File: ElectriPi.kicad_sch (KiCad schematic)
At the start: 35 parts, among them J1 2444, J2 JST XH 01x02, J3 JST XH 01x02, J6 Raspberry_Pi_2_3, J8 JST XH 01x02, Q1 30V 4A 44mΩ, Q2 50nA 150V 200mW 200mA, Q3 30V 4A 44mΩ, U1 XL4015

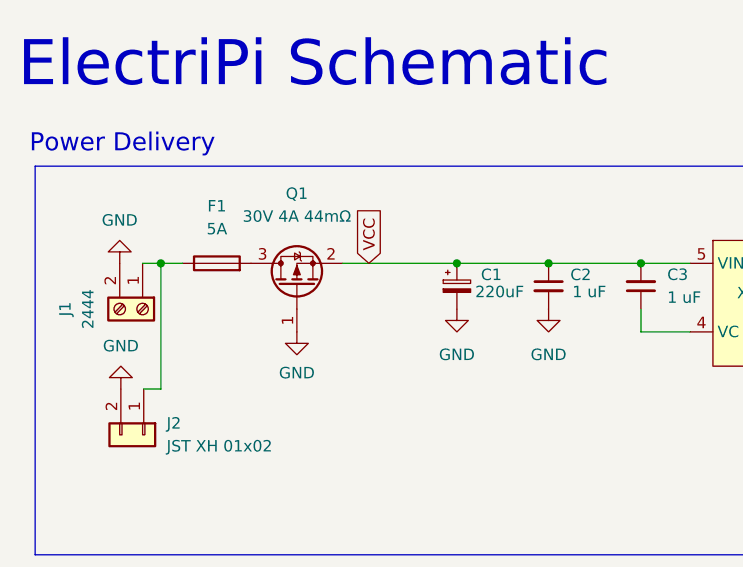
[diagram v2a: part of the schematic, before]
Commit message: Adding ICL footprint and schematic symbol
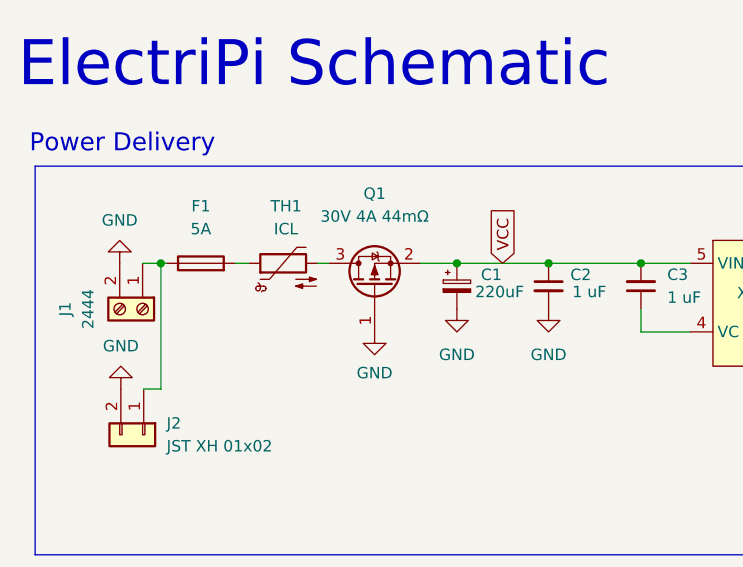
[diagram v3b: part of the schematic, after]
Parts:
- added TH1: ICL, Inrush_Limiter:5_OR_7pt5_PITCH_ICL, symbol Device:Thermistor_NTC
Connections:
- net at F1.2: now also TH1.1; no longer Q1.3 (D)
- new net: Q1.3 (D), TH1.2
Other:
- moved on the sheet: F1, Q1
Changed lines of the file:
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@@
     (stroke (width 0) (type default) (color 0 0 0 0))
   )
-  (wire (pts (xy 31.115 43.18) (xy 33.528 43.18))
+  (wire (pts (xy 31.115 43.18) (xy 31.75 43.18))
     (stroke (width 0) (type default) (color 0 0 0 0))
   )
@@
     (stroke (width 0) (type default) (color 0 0 0 0))
   )
-  (wire (pts (xy 51.308 43.18) (xy 64.008 43.18))
+  (wire (pts (xy 59.944 43.18) (xy 64.008 43.18))
     (stroke (width 0) (type default) (color 0 0 0 0))
   )
@@
     (stroke (width 0) (type default) (color 0 0 0 0))
   )
+  (wire (pts (xy 48.514 43.18) (xy 49.784 43.18))
+    (stroke (width 0) (type default) (color 0 0 0 0))
+  )
   (polyline (pts (xy 17.78 167.005) (xy 55.88 167.005))
     (stroke (width 0) (type default) (color 0 0 0 0))
@@
   )
   (wire (pts (xy 84.455 43.18) (xy 89.916 43.18))
+    (stroke (width 0) (type default) (color 0 0 0 0))
+  )
+  (wire (pts (xy 39.37 43.18) (xy 40.894 43.18))
     (stroke (width 0) (type default) (color 0 0 0 0))
   )
@@
     )
   )
-  (global_label "VCC" (shape input) (at 54.229 43.18 90) (fields_autoplaced)
+  (global_label "VCC" (shape input) (at 69.088 43.18 90) (fields_autoplaced)
     (effects (font (size 1.27 1.27)) (justify left))
-    (property "Intersheet References" "${INTERSHEET_REFS}" (id 0) (at 54.1496 37.1383 90)
+    (property "Intersheet References" "${INTERSHEET_REFS}" (id 0) (at 69.0086 37.1383 90)
       (effects (font (size 1.27 1.27)) (justify left) hide)
     )
@@
     (pin "2")
   )
-  (symbol (lib_id "power:GND") (at 46.228 50.8 0) (unit 1)
-    (in_bom yes) (on_board yes) (fields_autoplaced)
-    (property "Reference" "#PWR02" (id 0) (at 46.228 57.15 0)
-      (effects (font (size 1.27 1.27)) hide)
-    )
-    (property "Value" "GND" (id 1) (at 46.228 55.372 0))
-    (property "Footprint" "" (id 2) (at 46.228 50.8 0)
-      (effects (font (size 1.27 1.27)) hide)
-    )
-    (property "Datasheet" "" (id 3) (at 46.228 50.8 0)
-      (effects (font (size 1.27 1.27)) hide)
-    )
-    (pin "1")
+  (symbol (lib_id "power:GND") (at 54.864 50.8 0) (unit 1)
+    (in_bom yes) (on_board yes) (fields_autoplaced)
+    (property "Reference" "#PWR02" (id 0) (at 54.864 57.15 0)
+      (effects (font (size 1.27 1.27)) hide)
+    )
+    (property "Value" "GND" (id 1) (at 54.864 55.372 0))
+    (property "Footprint" "" (id 2) (at 54.864 50.8 0)
+      (effects (font (size 1.27 1.27)) hide)
+    )
+    (property "Datasheet" "" (id 3) (at 54.864 50.8 0)
+      (effects (font (size 1.27 1.27)) hide)
+    )
+    (pin "1")
+  )
+  (symbol (lib_id "Device:Thermistor_NTC") (at 44.704 43.18 90) (unit 1)
+    (in_bom yes) (on_board yes) (fields_autoplaced)
+    (property "Reference" "TH1" (id 0) (at 45.0215 36.83 90))
+    (property "Value" "ICL" (id 1) (at 45.0215 39.37 90))
+    (property "Footprint" "Inrush_Limiter:5_OR_7pt5_PITCH_ICL" (id 2) (at 43.434 43.18 0)
+      (effects (font (size 1.27 1.27)) hide)
+    )
+    (property "Datasheet" "~" (id 3) (at 43.434 43.18 0)
+      (effects (font (size 1.27 1.27)) hide)
+    )
+    (pin "1")
+    (pin "2")
   )
   (symbol (lib_id "power:GND") (at 29.083 150.622 270) (unit 1)
@@
     (pin "5")
   )
-  (symbol (lib_id "Device:Fuse") (at 37.338 43.18 90) (unit 1)
-    (in_bom yes) (on_board yes) (fields_autoplaced)
-    (property "Reference" "F1" (id 0) (at 37.338 36.83 90))
-    (property "Value" "5A" (id 1) (at 37.338 39.37 90))
-    (property "Footprint" "Fuse:Fuse_Littelfuse-NANO2-451_453" (id 2) (at 37.338 44.958 90)
-      (effects (font (size 1.27 1.27)) hide)
-    )
-    (property "Datasheet" "~" (id 3) (at 37.338 43.18 0)
-      (effects (font (size 1.27 1.27)) hide)
-    )
-    (property "LCSC" "C108518" (id 4) (at 37.338 43.18 90)
-      (effects (font (size 1.27 1.27)) hide)
-    )
-    (property "PCBway" "" (id 5) (at 37.338 43.18 0)
-      (effects (font (size 1.27 1.27)) hide)
-    )
-    (property "abv.Footprint" "" (id 6) (at 37.338 43.18 0)
-      (effects (font (size 1.27 1.27)) hide)
-    )
-    (property "ManfNum" "" (id 7) (at 37.338 43.18 0)
+  (symbol (lib_id "Device:Fuse") (at 35.56 43.18 90) (unit 1)
+    (in_bom yes) (on_board yes) (fields_autoplaced)
+    (property "Reference" "F1" (id 0) (at 35.56 36.83 90))
+    (property "Value" "5A" (id 1) (at 35.56 39.37 90))
+    (property "Footprint" "Fuse:Fuse_Littelfuse-NANO2-451_453" (id 2) (at 35.56 44.958 90)
+      (effects (font (size 1.27 1.27)) hide)
+    )
+    (property "Datasheet" "~" (id 3) (at 35.56 43.18 0)
+      (effects (font (size 1.27 1.27)) hide)
+    )
+    (property "LCSC" "C108518" (id 4) (at 35.56 43.18 90)
+      (effects (font (size 1.27 1.27)) hide)
+    )
+    (property "PCBway" "" (id 5) (at 35.56 43.18 0)
+      (effects (font (size 1.27 1.27)) hide)
+    )
+    (property "abv.Footprint" "" (id 6) (at 35.56 43.18 0)
+      (effects (font (size 1.27 1.27)) hide)
+    )
+    (property "ManfNum" "" (id 7) (at 35.56 43.18 0)
       (effects (font (size 1.27 1.27)) hide)
     )
@@
     (pin "1")
   )
-  (symbol (lib_id "Transistor_FET:AO3401A") (at 46.228 45.72 90) (unit 1)
-    (in_bom yes) (on_board yes) (fields_autoplaced)
-    (property "Reference" "Q1" (id 0) (at 46.228 35.433 90))
-    (property "Value" "30V 4A 44mΩ" (id 1) (at 46.228 37.973 90))
-    (property "Footprint" "Package_TO_SOT_SMD:SOT-23" (id 2) (at 48.133 40.64 0)
+  (symbol (lib_id "Transistor_FET:AO3401A") (at 54.864 45.72 90) (unit 1)
+    (in_bom yes) (on_board yes) (fields_autoplaced)
+    (property "Reference" "Q1" (id 0) (at 54.864 35.433 90))
+    (property "Value" "30V 4A 44mΩ" (id 1) (at 54.864 37.973 90))
+    (property "Footprint" "Package_TO_SOT_SMD:SOT-23" (id 2) (at 56.769 40.64 0)
       (effects (font (size 1.27 1.27) italic) (justify left) hide)
     )
-    (property "Datasheet" "http://www.aosmd.com/pdfs/datasheet/AO3401A.pdf" (id 3) (at 46.228 45.72 0)
+    (property "Datasheet" "http://www.aosmd.com/pdfs/datasheet/AO3401A.pdf" (id 3) (at 54.864 45.72 0)
       (effects (font (size 1.27 1.27)) (justify left) hide)
     )
-    (property "LCSC" "C15127" (id 4) (at 46.228 45.72 0)
-      (effects (font (size 1.27 1.27)) hide)
-    )
-    (property "ManfNum" "AO3401A" (id 5) (at 46.228 45.72 0)
-      (effects (font (size 1.27 1.27)) hide)
-    )
-    (property "abv.Footprint" "SOT-23" (id 6) (at 46.228 45.72 0)
+    (property "LCSC" "C15127" (id 4) (at 54.864 45.72 0)
+      (effects (font (size 1.27 1.27)) hide)
+    )
+    (property "ManfNum" "AO3401A" (id 5) (at 54.864 45.72 0)
+      (effects (font (size 1.27 1.27)) hide)
+    )
+    (property "abv.Footprint" "SOT-23" (id 6) (at 54.864 45.72 0)
       (effects (font (size 1.27 1.27)) hide)
     )
@@
       (reference "R10") (unit 1) (value "10K") (footprint "Resistor_SMD:R_0603_1608Metric")
     )
+    (path "/6bddfc29-f374-41df-b0b6-4faa72e48167"
+      (reference "TH1") (unit 1) (value "ICL") (footprint "Inrush_Limiter:5_OR_7pt5_PITCH_ICL")
+    )
     (path "/b1afdc82-ee5a-4cef-b119-9cb72898d220"

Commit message: adding test points
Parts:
- added TP1, TP2, TP3, TP4, TP5: TestPoint, TestPoint:TestPoint_Pad_D1.5mm, symbol Connector:TestPoint
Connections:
- net +5V: now also TP1.1
- net 5V_PI: now also TP5.1
- net VCC: now also TP4.1
- net at F1.1, J1.1 (Pin_1), J2.1 (Pin_1): now also TP2.1
- net at Q1.3 (D), TH1.2: now also TP3.1
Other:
- note removed: "add test points add 5V barrier block"
- moved on the sheet: F1, J1, J2, TH1

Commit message: small BOM updates
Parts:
- J1: LCSC (none) -> C123214
- J2, J3, J8: LCSC (none) -> C492456
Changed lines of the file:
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@@
       (effects (font (size 1.27 1.27)) hide)
     )
-    (property "LCSC" "" (id 4) (at 146.05 93.98 90)
+    (property "LCSC" "C492456" (id 4) (at 146.05 93.98 90)
       (effects (font (size 1.27 1.27)) hide)
     )
@@
       (effects (font (size 1.27 1.27)) hide)
     )
-    (property "LCSC" "" (id 4) (at 27.178 48.26 0)
+    (property "LCSC" "C123214" (id 4) (at 27.178 48.26 0)
       (effects (font (size 1.27 1.27)) hide)
     )
@@
     )
     (property "Datasheet" "~" (id 3) (at 27.178 62.738 0)
+      (effects (font (size 1.27 1.27)) hide)
+    )
+    (property "LCSC" "C492456" (id 4) (at 27.178 62.738 0)
       (effects (font (size 1.27 1.27)) hide)
     )
@@
       (effects (font (size 1.27 1.27)) hide)
     )
+    (property "LCSC" "C492456" (id 5) (at 161.925 151.765 0)
+      (effects (font (size 1.27 1.27)) hide)
+    )

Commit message: Adding Mouser part number for ICL
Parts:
- TH1: Mouser (none) -> 871-B57238S0709M000
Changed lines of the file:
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@@
       (effects (font (size 1.27 1.27)) hide)
     )
-    (property "Datasheet" "~" (id 3) (at 40.894 43.18 0)
+    (property "Datasheet" "https://product.tdk.com/system/files/dam/doc/product/protection/current/ntc-limiter/data_sheet/50/db/icl_16/s238.pdf" (id 3) (at 40.894 43.18 0)
       (effects (font (size 1.27 1.27)) hide)
     )
+    (property "Mouser" " 871-B57238S0709M000" (id 4) (at 42.164 43.18 90)
+      (effects (font (size 1.27 1.27)) hide)
+    )

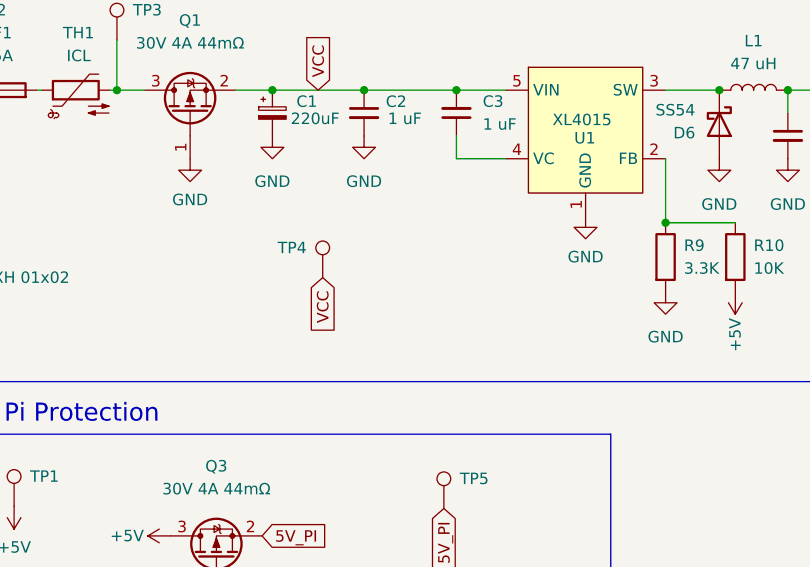
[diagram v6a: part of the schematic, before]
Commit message: adding GND test point
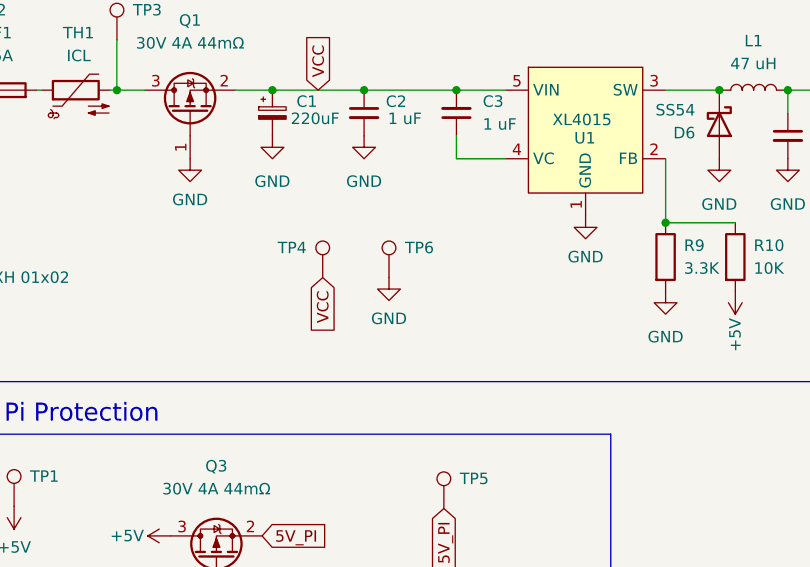
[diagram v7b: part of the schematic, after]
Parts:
- added TP6: TestPoint, TestPoint:TestPoint_Pad_D1.5mm, symbol Connector:TestPoint
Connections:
- net GND: now also TP6.1
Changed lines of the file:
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@@
+    (pin "1")
+  )
+  (symbol (lib_id "power:GND") (at 76.962 64.008 0) (unit 1)
+    (in_bom yes) (on_board yes) (fields_autoplaced)
+    (property "Reference" "#PWR010" (id 0) (at 76.962 70.358 0)
+      (effects (font (size 1.27 1.27)) hide)
+    )
+    (property "Value" "GND" (id 1) (at 76.962 68.58 0))
+    (property "Footprint" "" (id 2) (at 76.962 64.008 0)
+      (effects (font (size 1.27 1.27)) hide)
+    )
+    (property "Datasheet" "" (id 3) (at 76.962 64.008 0)
+      (effects (font (size 1.27 1.27)) hide)
+    )
     (pin "1")
   )
@@
     )
     (property "Datasheet" "~" (id 3) (at 92.075 183.515 0)
+      (effects (font (size 1.27 1.27)) hide)
+    )
+    (pin "1")
+  )
+  (symbol (lib_id "Connector:TestPoint") (at 76.962 64.008 0) (unit 1)
+    (in_bom yes) (on_board yes)
+    (property "Reference" "TP6" (id 0) (at 78.74 60.706 0)
+      (effects (font (size 1.27 1.27)) (justify left))
+    )
+    (property "Value" "TestPoint" (id 1) (at 78.74 61.9759 0)
+      (effects (font (size 1.27 1.27)) (justify left) hide)
+    )
+    (property "Footprint" "TestPoint:TestPoint_Pad_D1.5mm" (id 2) (at 82.042 64.008 0)
+      (effects (font (size 1.27 1.27)) hide)
+    )
+    (property "Datasheet" "~" (id 3) (at 82.042 64.008 0)
       (effects (font (size 1.27 1.27)) hide)
     )
@@
       (reference "#PWR09") (unit 1) (value "GND") (footprint "")
     )
+    (path "/374ac4ca-2900-4019-b85a-f241fc7de838"
+      (reference "#PWR010") (unit 1) (value "GND") (footprint "")
+    )
     (path "/e82c6728-328a-4fb4-b819-3d2b4377817e"
       (reference "#PWR011") (unit 1) (value "GND") (footprint "")
@@
       (reference "TP5") (unit 1) (value "TestPoint") (footprint "TestPoint:TestPoint_Pad_D1.5mm")
     )
+    (path "/49903123-4398-48a2-9b23-5a55ab00fec6"
+      (reference "TP6") (unit 1) (value "TestPoint") (footprint "TestPoint:TestPoint_Pad_D1.5mm")
+    )
     (path "/b1afdc82-ee5a-4cef-b119-9cb72898d220"

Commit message: Back Silkscreen Adjustments
Test point reference labels now hidden.
Adjusted credentials to match ElectriPi Mini
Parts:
- TH1: ManfNum (none) -> 871-B57238S0709M000
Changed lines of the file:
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@@
+      (effects (font (size 1.27 1.27)) hide)
+    )
+    (property "ManfNum" " 871-B57238S0709M000" (id 5) (at 42.164 43.18 0)
       (effects (font (size 1.27 1.27)) hide)
     )
